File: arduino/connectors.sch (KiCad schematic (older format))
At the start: 4 parts

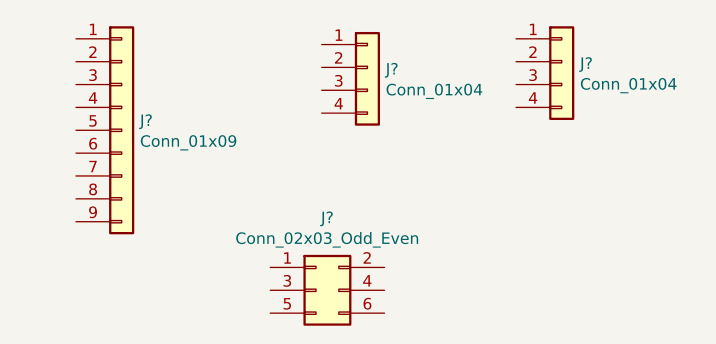
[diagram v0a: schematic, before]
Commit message: Create component + add
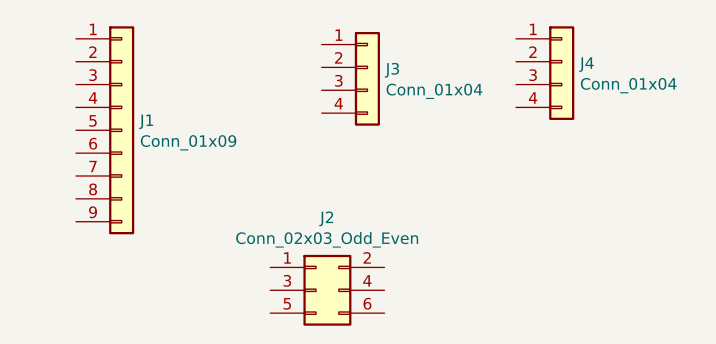
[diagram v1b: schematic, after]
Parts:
- J1: renamed from J?; footprint (none) -> Connector_PinSocket_2.54mm:PinSocket_1x09_P2.54mm_Vertical
- J2: renamed from J?; footprint (none) -> Connector_PinSocket_2.54mm:PinSocket_2x03_P2.54mm_Vertical
- J3, J4: renamed from J?; footprint (none) -> Connector_PinSocket_2.54mm:PinSocket_1x04_P2.54mm_Vertical
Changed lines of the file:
@@
 $EndDescr
 $Comp
-L Connector_Generic:Conn_01x09 J?
+L Connector_Generic:Conn_01x09 J1
 U 1 1 61739C81
 P 3650 3050
-F 0 "J?" H 3730 3092 50  0000 L CNN
+F 0 "J1" H 3730 3092 50  0000 L CNN
 F 1 "Conn_01x09" H 3730 3001 50  0000 L CNN
-F 2 "" H 3650 3050 50  0001 C CNN
+F 2 "Connector_PinSocket_2.54mm:PinSocket_1x09_P2.54mm_Vertical" H 3650 3050 50  0001 C CNN
 F 3 "~" H 3650 3050 50  0001 C CNN
 	1    3650 3050
@@
 $EndComp
 $Comp
-L Connector_Generic:Conn_01x04 J?
+L Connector_Generic:Conn_01x04 J3
 U 1 1 6173A5E1
 P 4725 2775
-F 0 "J?" H 4805 2767 50  0000 L CNN
+F 0 "J3" H 4805 2767 50  0000 L CNN
 F 1 "Conn_01x04" H 4805 2676 50  0000 L CNN
-F 2 "" H 4725 2775 50  0001 C CNN
+F 2 "Connector_PinSocket_2.54mm:PinSocket_1x04_P2.54mm_Vertical" H 4725 2775 50  0001 C CNN
 F 3 "~" H 4725 2775 50  0001 C CNN
 	1    4725 2775
@@
 $EndComp
 $Comp
-L Connector_Generic:Conn_02x03_Odd_Even J?
+L Connector_Generic:Conn_02x03_Odd_Even J2
 U 1 1 6173AF95
 P 4500 3750
-F 0 "J?" H 4550 4067 50  0000 C CNN
+F 0 "J2" H 4550 4067 50  0000 C CNN
 F 1 "Conn_02x03_Odd_Even" H 4550 3976 50  0000 C CNN
-F 2 "" H 4500 3750 50  0001 C CNN
+F 2 "Connector_PinSocket_2.54mm:PinSocket_2x03_P2.54mm_Vertical" H 4500 3750 50  0001 C CNN
 F 3 "~" H 4500 3750 50  0001 C CNN
 	1    4500 3750
@@
 $EndComp
 $Comp
-L Connector_Generic:Conn_01x04 J?
+L Connector_Generic:Conn_01x04 J4
 U 1 1 6173BFDD
 P 5575 2750
-F 0 "J?" H 5655 2742 50  0000 L CNN
+F 0 "J4" H 5655 2742 50  0000 L CNN
 F 1 "Conn_01x04" H 5655 2651 50  0000 L CNN
-F 2 "" H 5575 2750 50  0001 C CNN
+F 2 "Connector_PinSocket_2.54mm:PinSocket_1x04_P2.54mm_Vertical" H 5575 2750 50  0001 C CNN
 F 3 "~" H 5575 2750 50  0001 C CNN
 	1    5575 2750

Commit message: Add component values
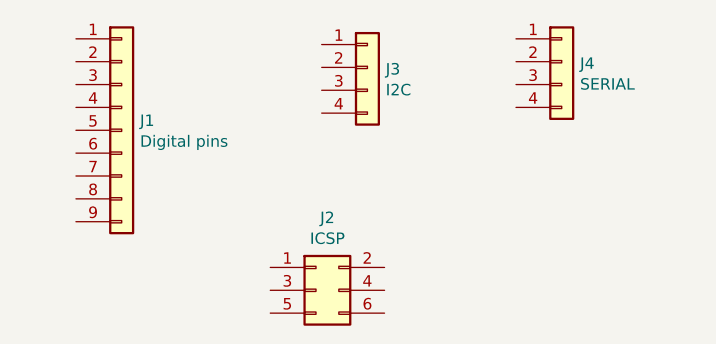
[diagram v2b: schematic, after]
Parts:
- J1: value Conn_01x09 -> Digital pins
- J2: value Conn_02x03_Odd_Even -> ICSP
- J3: value Conn_01x04 -> I2C
- J4: value Conn_01x04 -> SERIAL
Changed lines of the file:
@@
 P 3650 3050
 F 0 "J1" H 3730 3092 50  0000 L CNN
-F 1 "Conn_01x09" H 3730 3001 50  0000 L CNN
+F 1 "Digital pins" H 3730 3001 50  0000 L CNN
 F 2 "Connector_PinSocket_2.54mm:PinSocket_1x09_P2.54mm_Vertical" H 3650 3050 50  0001 C CNN
 F 3 "~" H 3650 3050 50  0001 C CNN
@@
 P 4725 2775
 F 0 "J3" H 4805 2767 50  0000 L CNN
-F 1 "Conn_01x04" H 4805 2676 50  0000 L CNN
+F 1 "I2C" H 4805 2676 50  0000 L CNN
 F 2 "Connector_PinSocket_2.54mm:PinSocket_1x04_P2.54mm_Vertical" H 4725 2775 50  0001 C CNN
 F 3 "~" H 4725 2775 50  0001 C CNN
@@
 P 4500 3750
 F 0 "J2" H 4550 4067 50  0000 C CNN
-F 1 "Conn_02x03_Odd_Even" H 4550 3976 50  0000 C CNN
+F 1 "ICSP" H 4550 3976 50  0000 C CNN
 F 2 "Connector_PinSocket_2.54mm:PinSocket_2x03_P2.54mm_Vertical" H 4500 3750 50  0001 C CNN
 F 3 "~" H 4500 3750 50  0001 C CNN
@@
 P 5575 2750
 F 0 "J4" H 5655 2742 50  0000 L CNN
-F 1 "Conn_01x04" H 5655 2651 50  0000 L CNN
+F 1 "SERIAL" H 5655 2651 50  0000 L CNN
 F 2 "Connector_PinSocket_2.54mm:PinSocket_1x04_P2.54mm_Vertical" H 5575 2750 50  0001 C CNN
 F 3 "~" H 5575 2750 50  0001 C CNN

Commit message: Done with schematic, start PCB
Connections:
- net D2: now reaches J1.1 (Pin_1)
- net D3: now reaches J1.2 (Pin_2)
- net D4: now reaches J1.3 (Pin_3)
- net D5: now reaches J1.4 (Pin_4)
- net D6: now reaches J1.5 (Pin_5)
- net D7: now reaches J1.6 (Pin_6)
- net D8: now reaches J1.7 (Pin_7)
- net GND: now reaches J1.8 (Pin_8)
- net GND: now also J2.6 (Pin_6), J3.3 (Pin_3), J4.3 (Pin_3)
- net VCC: now reaches J1.9 (Pin_9)
- net VCC: now also J2.2 (Pin_2), J3.4 (Pin_4), J4.4 (Pin_4)
- net SCL: now reaches J3.1 (Pin_1)
- net SCL: now also J2.3 (Pin_3)
- net SDA: now reaches J3.2 (Pin_2)
- net MISO: now reaches J2.1 (Pin_1)
- net MOSI: now reaches J2.4 (Pin_4)
- net RST: now reaches J2.5 (Pin_5)
- net TX: now reaches J4.1 (Pin_1)
- net RX: now reaches J4.2 (Pin_2)
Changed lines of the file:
@@
 $EndDescr
-$Comp
-L Connector_Generic:Conn_01x09 J1
-U 1 1 61739C81
-P 3650 3050
-F 0 "J1" H 3730 3092 50  0000 L CNN
-F 1 "Digital pins" H 3730 3001 50  0000 L CNN
-F 2 "Connector_PinSocket_2.54mm:PinSocket_1x09_P2.54mm_Vertical" H 3650 3050 50  0001 C CNN
-F 3 "~" H 3650 3050 50  0001 C CNN
-	1    3650 3050
-	1    0    0    -1
-$EndComp
 $Comp
 L Connector_Generic:Conn_01x04 J3
@@
 	1    0    0    -1
 $EndComp
+Text HLabel 4525 2675 0    50   BiDi ~ 0
+SCL
+Text HLabel 4525 2775 0    50   BiDi ~ 0
+SDA
+Text HLabel 5375 2750 0    50   Input ~ 0
+RX
+Text HLabel 4300 3650 0    50   Output ~ 0
+MISO
+Text HLabel 4300 3750 0    50   BiDi ~ 0
+SCL
+Text HLabel 4300 3850 0    50   Output ~ 0
+RST
+Text HLabel 4800 3650 2    50   Input ~ 0
+VCC
+Text HLabel 4800 3750 2    50   Input ~ 0
+MOSI
+Text HLabel 4800 3850 2    50   Input ~ 0
+GND
+Text HLabel 4525 2975 0    50   Input ~ 0
+VCC
 $Comp
 L Connector_Generic:Conn_01x04 J4
@@
 	1    0    0    -1
 $EndComp
+Text HLabel 5375 2950 0    50   Input ~ 0
+VCC
+Text HLabel 4525 2875 0    50   Input ~ 0
+GND
+Text HLabel 5375 2850 0    50   Input ~ 0
+GND
+Text HLabel 5375 2650 0    50   Output ~ 0
+TX
+$Comp
+L Connector_Generic:Conn_01x09 J1
+U 1 1 61739C81
+P 3650 3050
+F 0 "J1" H 3730 3092 50  0000 L CNN
+F 1 "Digital pins" H 3730 3001 50  0000 L CNN
+F 2 "Connector_PinSocket_2.54mm:PinSocket_1x09_P2.54mm_Vertical" H 3650 3050 50  0001 C CNN
+F 3 "~" H 3650 3050 50  0001 C CNN
+	1    3650 3050
+	1    0    0    -1
+$EndComp
+Text HLabel 3450 2650 0    50   BiDi ~ 0
+D2
+Text HLabel 3450 2750 0    50   BiDi ~ 0
+D3
+Text HLabel 3450 2850 0    50   BiDi ~ 0
+D4
+Text HLabel 3450 2950 0    50   BiDi ~ 0
+D5
+Text HLabel 3450 3050 0    50   BiDi ~ 0
+D6
+Text HLabel 3450 3150 0    50   BiDi ~ 0
+D7
+Text HLabel 3450 3250 0    50   BiDi ~ 0
+D8
+Text HLabel 3450 3350 0    50   Input ~ 0
+GND
+Text HLabel 3450 3450 0    50   Input ~ 0
+VCC
 $EndSCHEMATC
